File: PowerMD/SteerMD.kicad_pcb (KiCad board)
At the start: 2 copper layers, 75 x 88 mm, 202 parts, among them P1 SWD, P10 OUT_1, P11 ENC_0, P13 ENC_1, P14 I/O_1, P15 OUT_0, P3 CAN, P4 CAN, P5 SERIAL, P6 I/O_0, P7 FAN, P8 BATT_IN, P9 BATT_IN, Q1 MOSFET_N, Q2 MOSFET_N, Q3 MOSFET_N, Q4 MOSFET_N, Q5 MOSFET_N, Q6 MOSFET_N, Q7 MOSFET_N, Q8 MOSFET_N, SW1 RST, SW3 SW0, SW4 SW1, U1 MAX3051, U10 ACS758, U11 POWER_ON, U12 SI8274, U13 ACS758, U14 SI8274, U15 AZ1086H, U16 LOGO, U19 ADRESS, U2 AP3211, U3 STM32F405RG, U4 SI8274, U5 SI8900, U6 ADC_~RST, U7 BD9G101G, U8 SI8274, U9 BD33FA1, Y1 8MHz

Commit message: Power MD
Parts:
- moved R67 27.3 mm to (105.0, 107.8)
- moved R69 5.90 mm to (188.2, 101.9)
- moved C52 3.30 mm to (133.1, 1.35)
- moved R22 2.95 mm to (134.1, 89.6)
- moved R23 2.95 mm to (135.7, 89.6)
- moved R13 0.37 mm to (129.7, -1.95)
- moved R66 0.11 mm to (129.8, 2.87)
- moved R68 0.06 mm to (183.2, 17.2)
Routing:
- net +12P: track 24.5 -> 78.8 mm, vias 2 -> 10
- net Net-(R18-Pad2): track 0.00 -> 37.1 mm
- net /Motor0L_Tmp: track 0.00 -> 30.4 mm
- net +3V3: track 45.4 -> 75.1 mm, vias 8 -> 9
- net Net-(R17-Pad2): track 0.00 -> 25.5 mm
- net +BATT: track 98.4 -> 121.7 mm, vias 38 -> 39
- net GNDPWR: track 57.4 -> 77.3 mm, vias 33 -> 40
- net /CounterVoltage1: track 3.53 -> 16.1 mm, vias 0 -> 2
- net /CounterVoltage0: track 21.3 -> 33.6 mm, vias 0 -> 2
- net +3.3VP: track 37.3 -> 46.4 mm
- net /OUT1_R: track 10.9 -> 2.66 mm
- net Net-(C48-Pad1): track 0.00 -> 5.25 mm
- net Net-(C20-Pad1): track 0.00 -> 5.25 mm
- net Net-(C19-Pad1): track 0.00 -> 5.25 mm
- net Net-(C30-Pad1): track 0.00 -> 5.24 mm
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
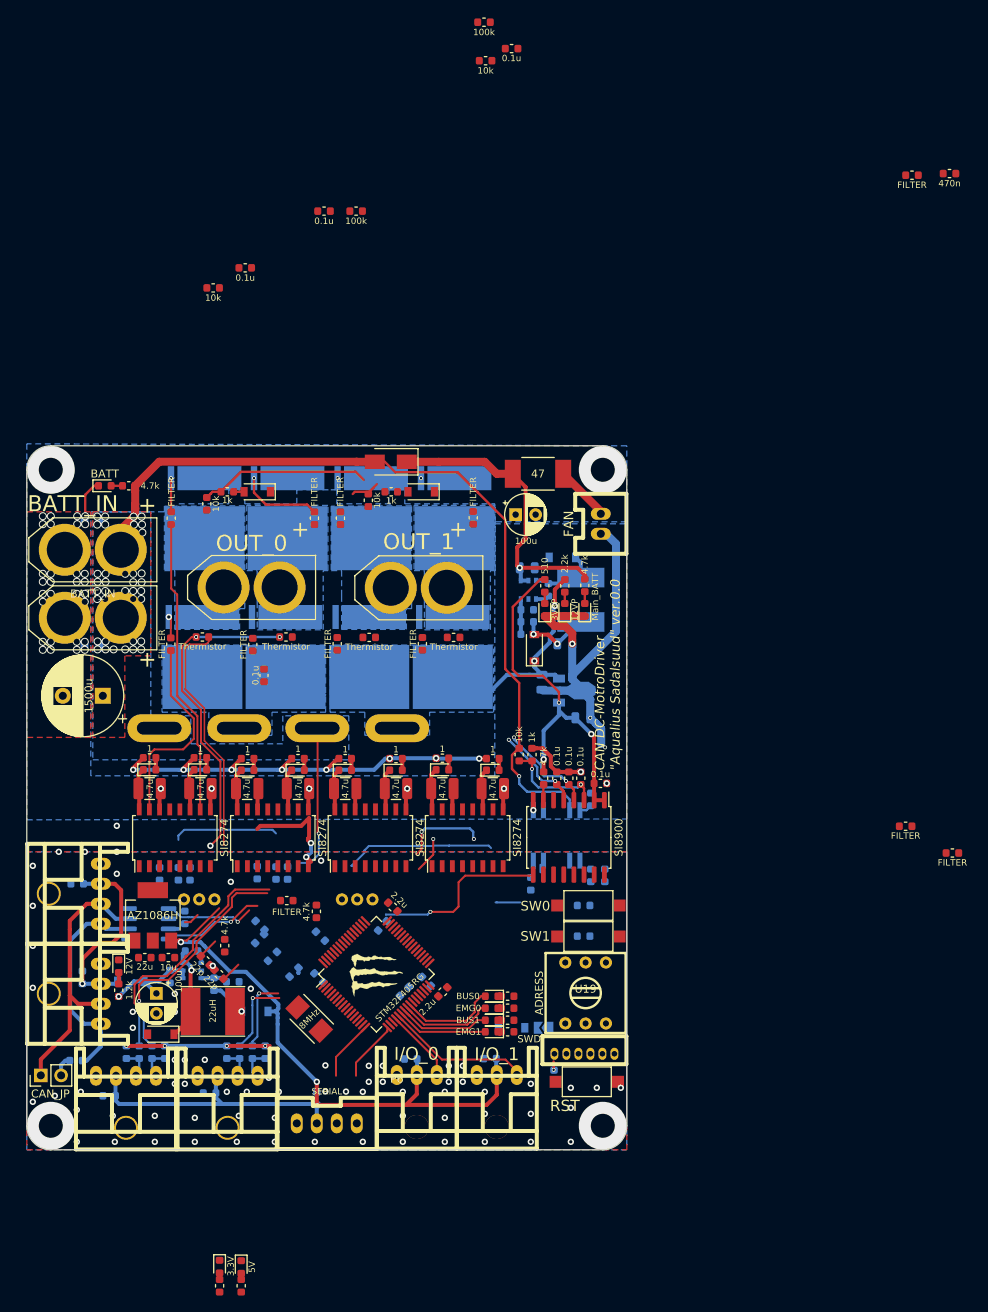
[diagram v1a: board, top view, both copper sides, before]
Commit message: サーミスタのピンアサインの決定
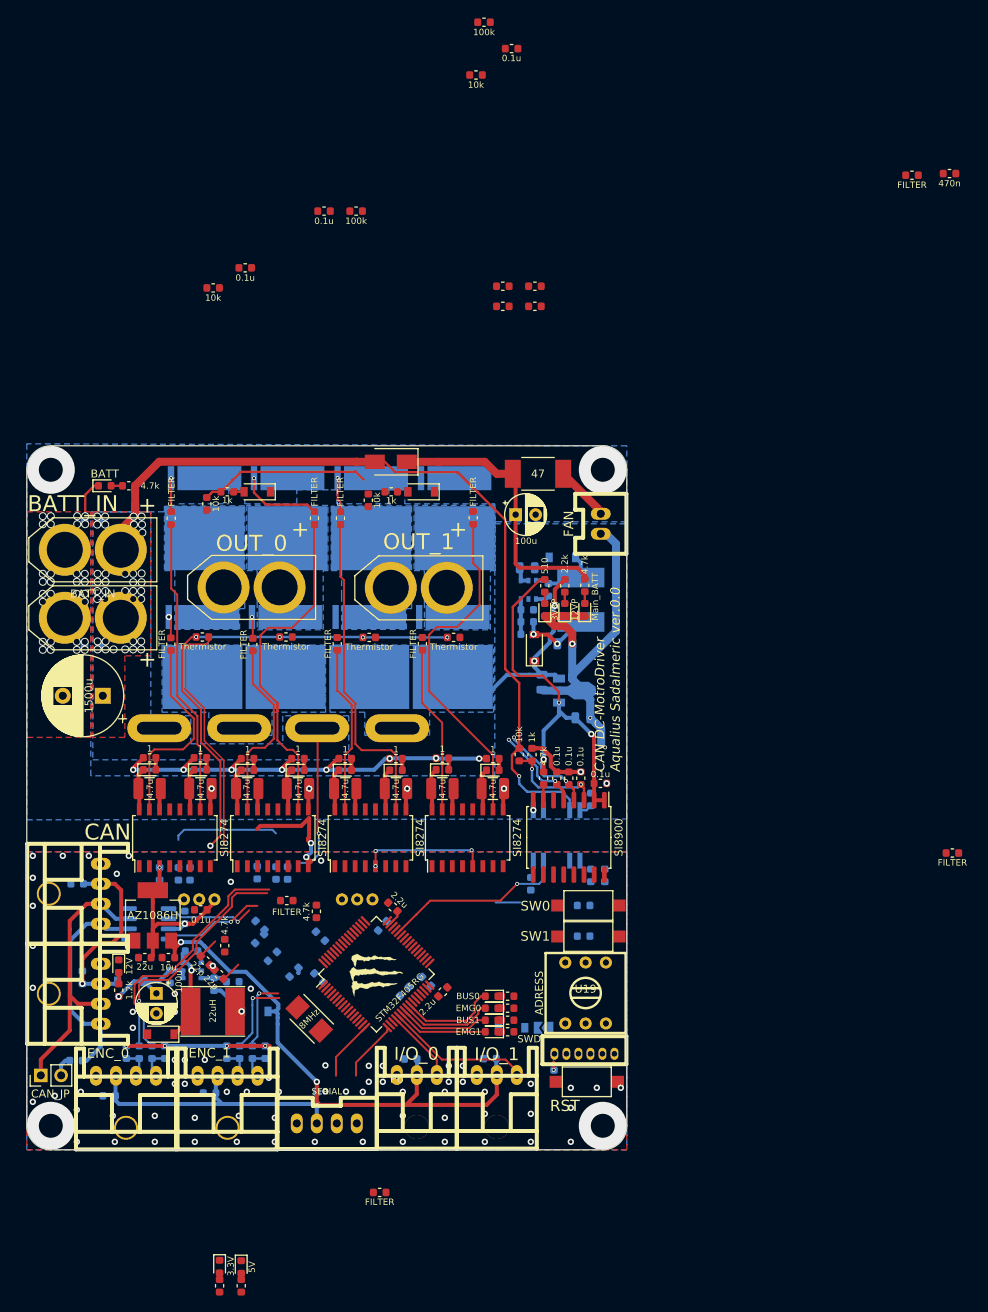
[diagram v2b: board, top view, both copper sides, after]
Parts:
- added C53: 0.1u, Capacitor_SMD:C_0603_1608Metric, F.Cu at (132.0, 31.1)
- added C54: 0.1u, Capacitor_SMD:C_0603_1608Metric, F.Cu at (132.0, 33.6)
- added C58: 0.1u, Capacitor_SMD:C_0603_1608Metric, F.Cu at (136.0, 31.1)
- added C59: 0.1u, Capacitor_SMD:C_0603_1608Metric, F.Cu at (136.0, 33.6)
- moved R52 80.1 mm to (116.6, 144.3)
- moved C36 30.3 mm to (94.2, 109.0), turned to 180 degrees
- moved R66 2.15 mm to (128.7, 4.65)
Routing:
- net Net-(R31-Pad2): track 0.00 -> 43.7 mm
- net Net-(R64-Pad2): track 0.00 -> 43.4 mm
- net +3V3: track 75.1 -> 118.0 mm, vias 9 -> 13
- net Net-(R54-Pad2): track 0.00 -> 40.7 mm
- net Net-(R30-Pad2): track 0.00 -> 23.1 mm
- net GND: track 22.7 -> 0.00 mm, vias 73 -> 72
- net Net-(R53-Pad2): track 0.00 -> 21.0 mm
- net Net-(R63-Pad2): track 0.00 -> 20.9 mm
- net /EN1: track 10.8 -> 16.0 mm, vias 2 -> 3
- net /PWM1_R: track 4.51 -> 0.00 mm, vias 1 -> 0
- net /PA11: track 18.8 -> 23.3 mm, vias 0 -> 1
- net Net-(Q4-PadG): track 0.00 -> 4.36 mm
- net +5V: track 107.2 -> 103.3 mm
- net /CounterVoltage1: track 16.1 -> 12.6 mm
- net Net-(Q5-PadG): track 0.00 -> 2.70 mm, vias 0 -> 1
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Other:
- board text added: "CAN DC-MotroDriver Aqualius Sadalmeric ver.0.0"
- board text removed: "CAN DC-MotroDriver "Aqualius Sadalsuud" ver.0.0"

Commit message: パワミMD
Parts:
- C34: footprint Capacitor_THT:CP_Radial_D10.0mm_P5.00mm -> Capacitor_THT:C_Radial_D12.5mm_H25.0mm_P5.00mm
- moved C34 1.06 mm to (82.0, 83.3)
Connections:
- net /LED4 renamed Net-(U3-Pad26)
- U3 pad 10: /Current1 -> /Motor1L_Tmp
- U3 pad 11: /Current0 -> /Motor1R_Tmp
- U3 pad 22: /LED0 -> Net-(U3-Pad22)
- U3 pad 23: /LED1 -> Net-(U3-Pad23)
- U3 pad 24: /LED2 -> /Current1
- U3 pad 25: /LED3 -> /Current0
- U3 pad 8: /Motor1_Tmp -> /Motor0L_Tmp
- U3 pad 9: /Motor1_Tmp -> /Motor0R_Tmp

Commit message: NT中の進捗
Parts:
- moved R61 0.24 mm to (115.2, 58.0)
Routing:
- net /Motor1L_Tmp: track 0.00 -> 39.6 mm
- net /Motor1R_Tmp: track 0.00 -> 34.9 mm
- net /Motor0R_Tmp: track 0.00 -> 33.7 mm
- net +BATT: track 121.7 -> 102.3 mm, vias 39 -> 38
- net Net-(R31-Pad2): track 43.7 -> 42.6 mm
- net GND: vias 72 -> 71
- net /OUT1_L: vias 0 -> 39
- net /OUT0_R: vias 0 -> 29
- net /OUT0_L: vias 0 -> 39
- net /MOTOR0_BATT: vias 0 -> 20
- added copper zone on F.Cu, net /MOTOR0_BATT
- added copper zone on F.Cu, net /OUT0_L
- added copper zone on F.Cu, net /OUT0_R
- added copper zone on F.Cu, net /OUT1_L

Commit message: ピン配置王幅変更
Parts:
- added C60: 0.1u, Capacitor_SMD:C_0603_1608Metric, F.Cu at (126.3, 143.1)
- added R70: FILTER, Resistor_SMD:R_0603_1608Metric, F.Cu at (126.3, 145.6)
- added TH5: Thermistor, Capacitor_SMD:C_0603_1608Metric, F.Cu at (130.3, 143.1)
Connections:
- net /PA15 renamed Net-(U3-Pad50)
- P14 pad 3: /PA5 -> /IO_1
- P6 pad 3: /PA4 -> /IO_0
- U3 pad 10: /Motor1L_Tmp -> Net-(U3-Pad10)
- U3 pad 11: /Motor1R_Tmp -> Net-(U3-Pad11)
- U3 pad 2: /ADR_2 -> Net-(U3-Pad2)
- U3 pad 20: /PA4 -> /Substrate_Temp
- U3 pad 21: /PA5 -> Net-(U3-Pad21)
- U3 pad 24: /Current1 -> Net-(U3-Pad24)
- U3 pad 25: /Current0 -> /Motor1L_Tmp
- U3 pad 26: Net-(U3-Pad26) -> /Motor1R_Tmp
- U3 pad 27: /SW0 -> Net-(U3-Pad27)
- U3 pad 29: /SW1 -> Net-(U3-Pad29)
- U3 pad 3: /ADR_4 -> Net-(U3-Pad3)
- U3 pad 4: /ADR_1 -> Net-(U3-Pad4)
- U3 pad 44: /PA11 -> Net-(U3-Pad44)
- U3 pad 45: Net-(U3-Pad45) -> /PA12
- U3 pad 58: /ADR_8 -> Net-(U3-Pad58)
- U3 pad 8: /Motor0L_Tmp -> /Motor0R_Tmp
- U3 pad 9: /Motor0R_Tmp -> /Motor0L_Tmp
- U6 pad 1: /PA11 -> /PA12
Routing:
- net /LED3: track 12.2 -> 0.00 mm
- net /LED2: track 11.7 -> 0.00 mm
- net /LED1: track 11.5 -> 0.00 mm
- net /LED0: track 11.4 -> 0.00 mm

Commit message: 2019/12/18
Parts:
- moved R64 0.80 mm to (129.1, 60.0)
- moved U10 0.30 mm to (94.0, 107.4)
- moved U13 0.30 mm to (113.8, 107.4)
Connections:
- C29 pad 1: +12P -> /MOTOR1_BATT
- D18 pad 1: +12P -> /MOTOR1_BATT
- R33 pad 2: +12P -> /MOTOR1_BATT
- U9 pad 3: +12P -> /MOTOR1_BATT
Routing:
- net +12P: track 78.8 -> 54.8 mm, vias 10 -> 8
- net /MOTOR1_BATT: track 0.00 -> 24.0 mm, vias 0 -> 42
- net Net-(Q8-PadG): track 0.00 -> 10.7 mm, vias 0 -> 1
- net Net-(Q7-PadG): track 0.00 -> 2.73 mm, vias 0 -> 1
- net Net-(Q3-PadG): track 0.00 -> 2.65 mm, vias 0 -> 1
- net /MOTOR0_BATT: vias 20 -> 37
- added copper zone on F.Cu, net /MOTOR1_BATT

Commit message: MD
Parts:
- C4, C52, C60, R13, R2, R65, R66: moved to B.Cu
- C50, C9: moved to F.Cu
- moved C47 123.0 mm to (108.9, 111.3), turned to 180 degrees
- moved R68 107.7 mm to (122.3, 106.1)
- moved R13 107.0 mm to (117.3, 104.3), turned to 270 degrees
- moved C52 103.0 mm to (132.1, 104.3), turned to 270 degrees
- moved R66 99.7 mm to (128.2, 104.3), turned to 270 degrees
- moved R65 84.2 mm to (129.6, 104.3), turned to 270 degrees
- moved C4 78.2 mm to (119.9, 104.3), turned to 270 degrees
- moved R2 75.8 mm to (116.0, 104.3), turned to 270 degrees
- moved R49 52.0 mm to (130.8, 116.8), turned to 0 degrees
- moved D34 48.6 mm to (128.3, 116.8), turned to 0 degrees
- moved R48 48.3 mm to (130.8, 119.3), turned to 0 degrees
- moved D33 45.0 mm to (128.4, 119.3), turned to 0 degrees
- moved R52 31.9 mm to (106.9, 114.0), turned to 180 degrees
- moved R70 23.0 mm to (127.7, 122.7)
- moved TH5 19.1 mm to (127.7, 124.2), turned to 180 degrees
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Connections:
- C29 pad 1: /MOTOR1_BATT -> +12P
- D18 pad 1: /MOTOR1_BATT -> +12P
- R33 pad 2: /MOTOR1_BATT -> +12P
- U3 pad 10: Net-(U3-Pad10) -> /Current0
- U3 pad 21: Net-(U3-Pad21) -> /ADR_1
- U3 pad 22: Net-(U3-Pad22) -> /ADR_4
- U3 pad 23: Net-(U3-Pad23) -> /ADR_2
- U3 pad 24: Net-(U3-Pad24) -> /Current1
- U3 pad 27: Net-(U3-Pad27) -> /ADR_8
- U3 pad 50: Net-(U3-Pad50) -> /LED0
- U3 pad 51: Net-(U3-Pad51) -> /LED1
- U3 pad 52: Net-(U3-Pad52) -> /LED2
- U3 pad 53: Net-(U3-Pad53) -> /LED3
- U9 pad 3: /MOTOR1_BATT -> +12P
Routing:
- net /PA5: track 18.1 -> 0.00 mm
- net +3V3: track 118.0 -> 127.5 mm
- net /PA4: track 9.12 -> 0.00 mm
- net /USART2_RX: track 7.66 -> 0.00 mm
- net /USART2_TX: track 7.56 -> 0.00 mm
- net /OSC_OUT: track 2.60 -> 0.00 mm
- net /OSC_IN: track 2.59 -> 0.00 mm
- net Net-(P7-Pad2): track 6.95 -> 9.00 mm
- net Net-(R64-Pad2): track 43.1 -> 44.2 mm
- net +BATT: track 102.3 -> 103.2 mm
- net +3.3VP: track 46.4 -> 47.0 mm
- net GND: vias 71 -> 70
- net /OUT1_R: vias 0 -> 25
- added copper zone on F.Cu, net /OUT1_R

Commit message: やる気がなくなった,ここまで
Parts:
- moved C1 1.12 mm to (105.0, 125.5)
- moved C3 0.76 mm to (107.8, 128.2)
- moved R4 0.35 mm to (141.8, 108.5)
- moved R5 0.30 mm to (141.8, 112.3)
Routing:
- net +5V: track 103.3 -> 130.5 mm
- net /SW1: track 0.00 -> 2.23 mm, vias 0 -> 1
- net /SW0: track 0.00 -> 2.17 mm, vias 0 -> 1
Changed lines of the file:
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@@
     (thickness 1.6)
     (drawings 42)
-    (tracks 1127)
+    (tracks 1147)
     (zones 0)
     (modules 209)
@@
   )
   (setup
-    (last_trace_width 0.25)
+    (last_trace_width 0.5)
     (user_trace_width 0.2)
     (user_trace_width 0.3)
@@
   )
   (module Capacitor_SMD:C_0603_1608Metric (layer F.Cu)
-    (at 104.25 124.75 315)
+    (at 105.043153 125.543153 315)
     (descr "Capacitor SMD 0603 (1608 Metric), square (rectangular) end terminal, IPC_7351 nominal, (Body size source: http://www.tortai-tech.com/upload/download/2011102023233369053.pdf), generated with kicad-footprint-generator")
     (tags capacitor)
@@
       (effects (font (size 1 1) (thickness 0.15)))
     )
-    (fp_text value 22p (at -2.474874 0 135) (layer F.SilkS)
+    (fp_text value 22p (at -2.535901 0 135) (layer F.SilkS)
       (effects (font (size 0.8 0.8) (thickness 0.15)))
     )
@@
   )
   (module Capacitor_SMD:C_0603_1608Metric (layer F.Cu)
-    (at 108.4 128.65 135)
+    (at 107.75 128.25 135)
     (descr "Capacitor SMD 0603 (1608 Metric), square (rectangular) end terminal, IPC_7351 nominal, (Body size source: http://www.tortai-tech.com/upload/download/2011102023233369053.pdf), generated with kicad-footprint-generator")
     (tags capacitor)
@@
       (effects (font (size 1 1) (thickness 0.15)))
     )
-    (fp_text value 22p (at 2.58094 -0.035355 135) (layer F.SilkS)
+    (fp_text value 22p (at 0.282843 -1.202082 135) (layer F.SilkS)
       (effects (font (size 0.8 0.8) (thickness 0.15)))
     )
@@
   )
   (module Resistor_SMD:R_0603_1608Metric (layer B.Cu)
-    (at 142.1 108.46 180)
+    (at 141.75 108.46 180)
     (descr "Resistor SMD 0603 (1608 Metric), square (rectangular) end terminal, IPC_7351 nominal, (Body size source: http://www.tortai-tech.com/upload/download/2011102023233369053.pdf), generated with kicad-footprint-generator")
     (tags resistor)
@@
   )
   (module Resistor_SMD:R_0603_1608Metric (layer B.Cu)
-    (at 142.1 112.29 180)
+    (at 141.8 112.29 180)
     (descr "Resistor SMD 0603 (1608 Metric), square (rectangular) end terminal, IPC_7351 nominal, (Body size source: http://www.tortai-tech.com/upload/download/2011102023233369053.pdf), generated with kicad-footprint-generator")
     (tags resistor)
@@
   (via (at 75.5 54) (size 6) (drill 3) (layers F.Cu B.Cu) (net 0))
   (via (at 144.5 54) (size 6) (drill 3) (layers F.Cu B.Cu) (net 0))
-  (via (at 127.5 70.5) (size 1.5) (drill 0.75) (layers F.Cu B.Cu) (net 109))
-  (via (at 127.65 67.25) (size 1.5) (drill 0.75) (layers F.Cu B.Cu) (net 109))
   (via (at 100.5 118.86) (size 0.8) (drill 0.4) (layers F.Cu B.Cu) (net 2))
   (via (at 146.75 131.25) (size 0.8) (drill 0.4) (layers F.Cu B.Cu) (net 2))
@@
   (segment (start 90.55 113.373003) (end 90.9875 113.810503) (width 0.5) (layer F.Cu) (net 23))
   (segment (start 90.55 112.85) (end 90.55 113.373003) (width 0.5) (layer F.Cu) (net 23))
+  (segment (start 142.5375 112.24) (end 142.5875 112.29) (width 0.5) (layer B.Cu) (net 23))
+  (segment (start 142.5375 108.46) (end 142.5375 112.24) (width 0.5) (layer B.Cu) (net 23))
+  (segment (start 131.1875 127.6) (end 131.1875 126.8125) (width 0.5) (layer B.Cu) (net 23))
+  (segment (start 131.1875 126.8125) (end 133.15 124.85) (width 0.5) (layer B.Cu) (net 23))
+  (segment (start 133.15 124.85) (end 133.15 116.5) (width 0.5) (layer B.Cu) (net 23))
+  (segment (start 133.15 116.5) (end 135.6 114.05) (width 0.5) (layer B.Cu) (net 23))
+  (segment (start 142.5875 112.865) (end 141.7025 113.75) (width 0.5) (layer B.Cu) (net 23))
+  (segment (start 142.5875 112.29) (end 142.5875 112.865) (width 0.5) (layer B.Cu) (net 23))
+  (segment (start 135.9 113.75) (end 135.6 114.05) (width 0.5) (layer B.Cu) (net 23))
+  (segment (start 141.7025 113.75) (end 135.9 113.75) (width 0.5) (layer B.Cu) (net 23))
   (segment (start 119.4375 91.55) (end 119.4375 90.1) (width 0.5) (layer F.Cu) (net 24))
   (segment (start 125.2375 91.5) (end 125.2375 90.05) (width 0.5) (layer F.Cu) (net 25))
@@
   (segment (start 142.7 61.9) (end 142.2 61.9) (width 1) (layer F.Cu) (net 47))
   (segment (start 142.2 61.9) (end 139.55 59.25) (width 1) (layer F.Cu) (net 47))
+  (via (at 140.05 108.45) (size 0.5) (drill 0.3) (layers F.Cu B.Cu) (net 49))
+  (segment (start 140.9625 108.46) (end 140.06 108.46) (width 0.25) (layer B.Cu) (net 49))
+  (segment (start 140.06 108.46) (end 140.05 108.45) (width 0.25) (layer B.Cu) (net 49))
+  (segment (start 138.81 108.45) (end 138.8 108.46) (width 0.25) (layer F.Cu) (net 49))
+  (segment (start 140.05 108.45) (end 138.81 108.45) (width 0.25) (layer F.Cu) (net 49))
+  (via (at 140.05 112.3) (size 0.5) (drill 0.3) (layers F.Cu B.Cu) (net 50))
+  (segment (start 141.0125 112.29) (end 140.06 112.29) (width 0.25) (layer B.Cu) (net 50))
+  (segment (start 140.06 112.29) (end 140.05 112.3) (width 0.25) (layer B.Cu) (net 50))
+  (segment (start 138.84 112.3) (end 138.8 112.34) (width 0.25) (layer F.Cu) (net 50))
+  (segment (start 140.05 112.3) (end 138.84 112.3) (width 0.25) (layer F.Cu) (net 50))
   (segment (start 91.45 99.725) (end 92.175 99) (width 0.25) (layer B.Cu) (net 55))
   (segment (start 91.45 100.2625) (end 91.45 99.725) (width 0.25) (layer B.Cu) (net 55))
@@
   (segment (start 123.05 92.1125) (end 123.6625 91.5) (width 0.5) (layer F.Cu) (net 106))
   (segment (start 123.05 93.85) (end 123.05 92.1125) (width 0.5) (layer F.Cu) (net 106))
+  (via (at 127.5 70.5) (size 1.5) (drill 0.75) (layers F.Cu B.Cu) (net 109))
+  (via (at 127.65 67.25) (size 1.5) (drill 0.75) (layers F.Cu B.Cu) (net 109))
   (via (at 123 72) (size 1.5) (drill 0.75) (layers F.Cu B.Cu) (net 109))
   (via (at 127.5 72) (size 1.5) (drill 0.75) (layers F.Cu B.Cu) (net 109))
